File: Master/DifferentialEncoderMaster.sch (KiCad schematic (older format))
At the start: 7 parts

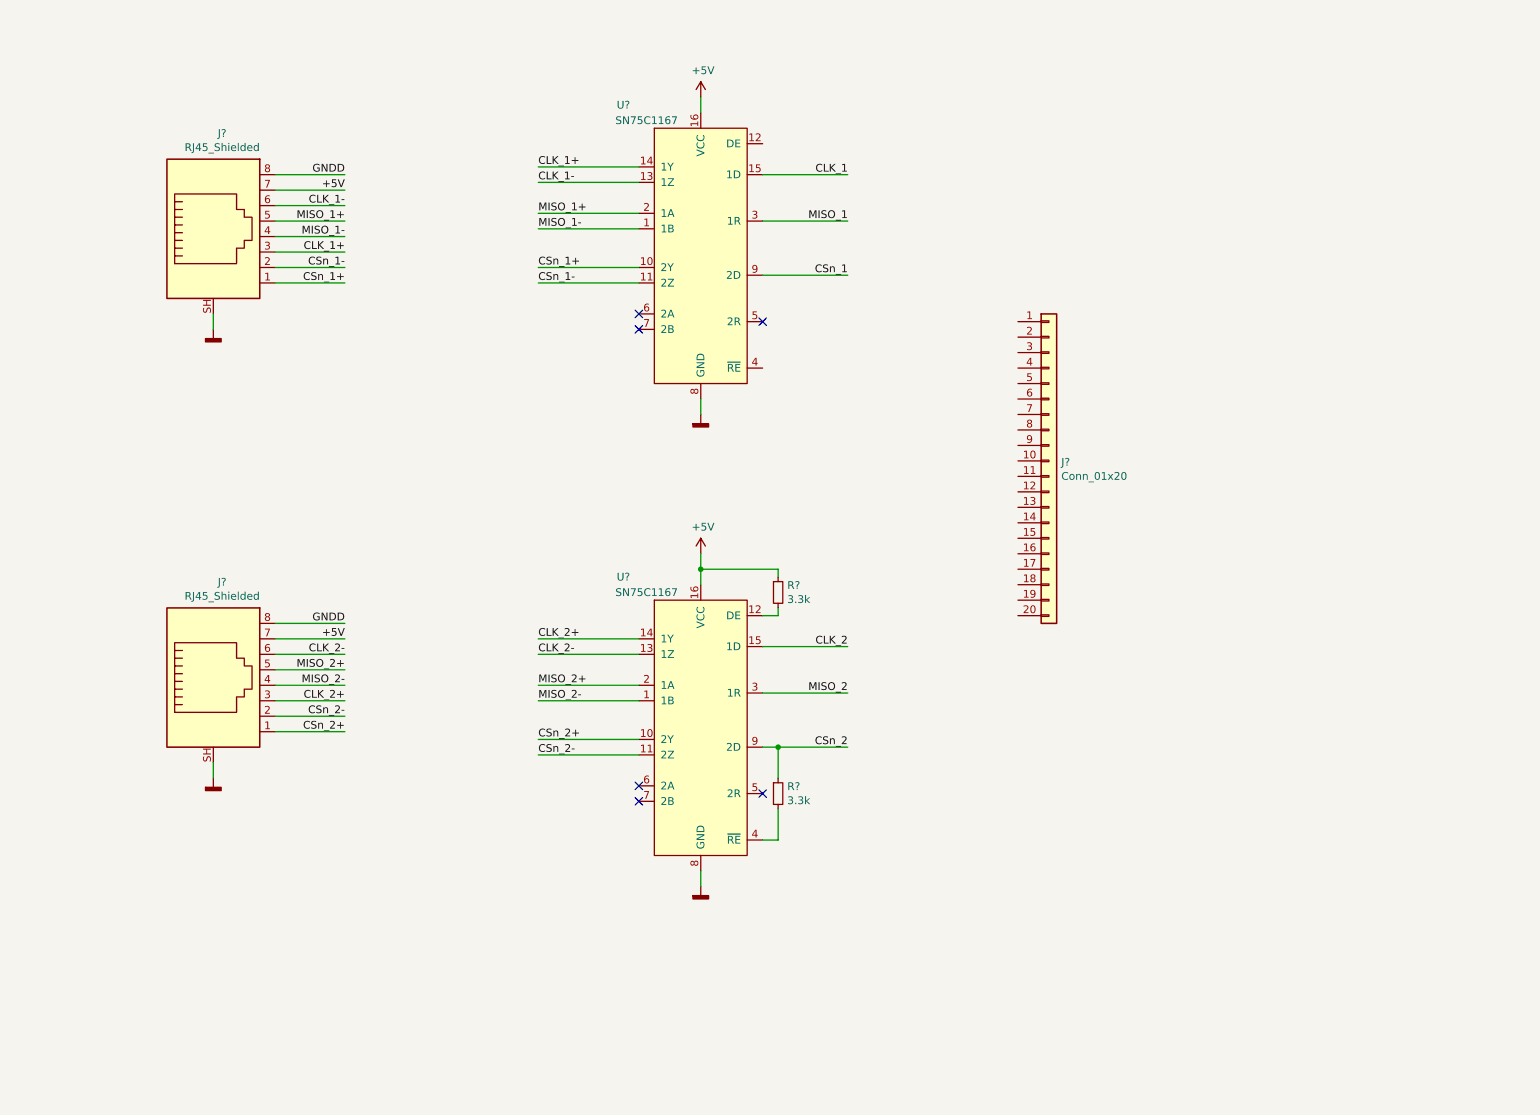
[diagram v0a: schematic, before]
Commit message: Make ODrive side full board length, add diff. incremental
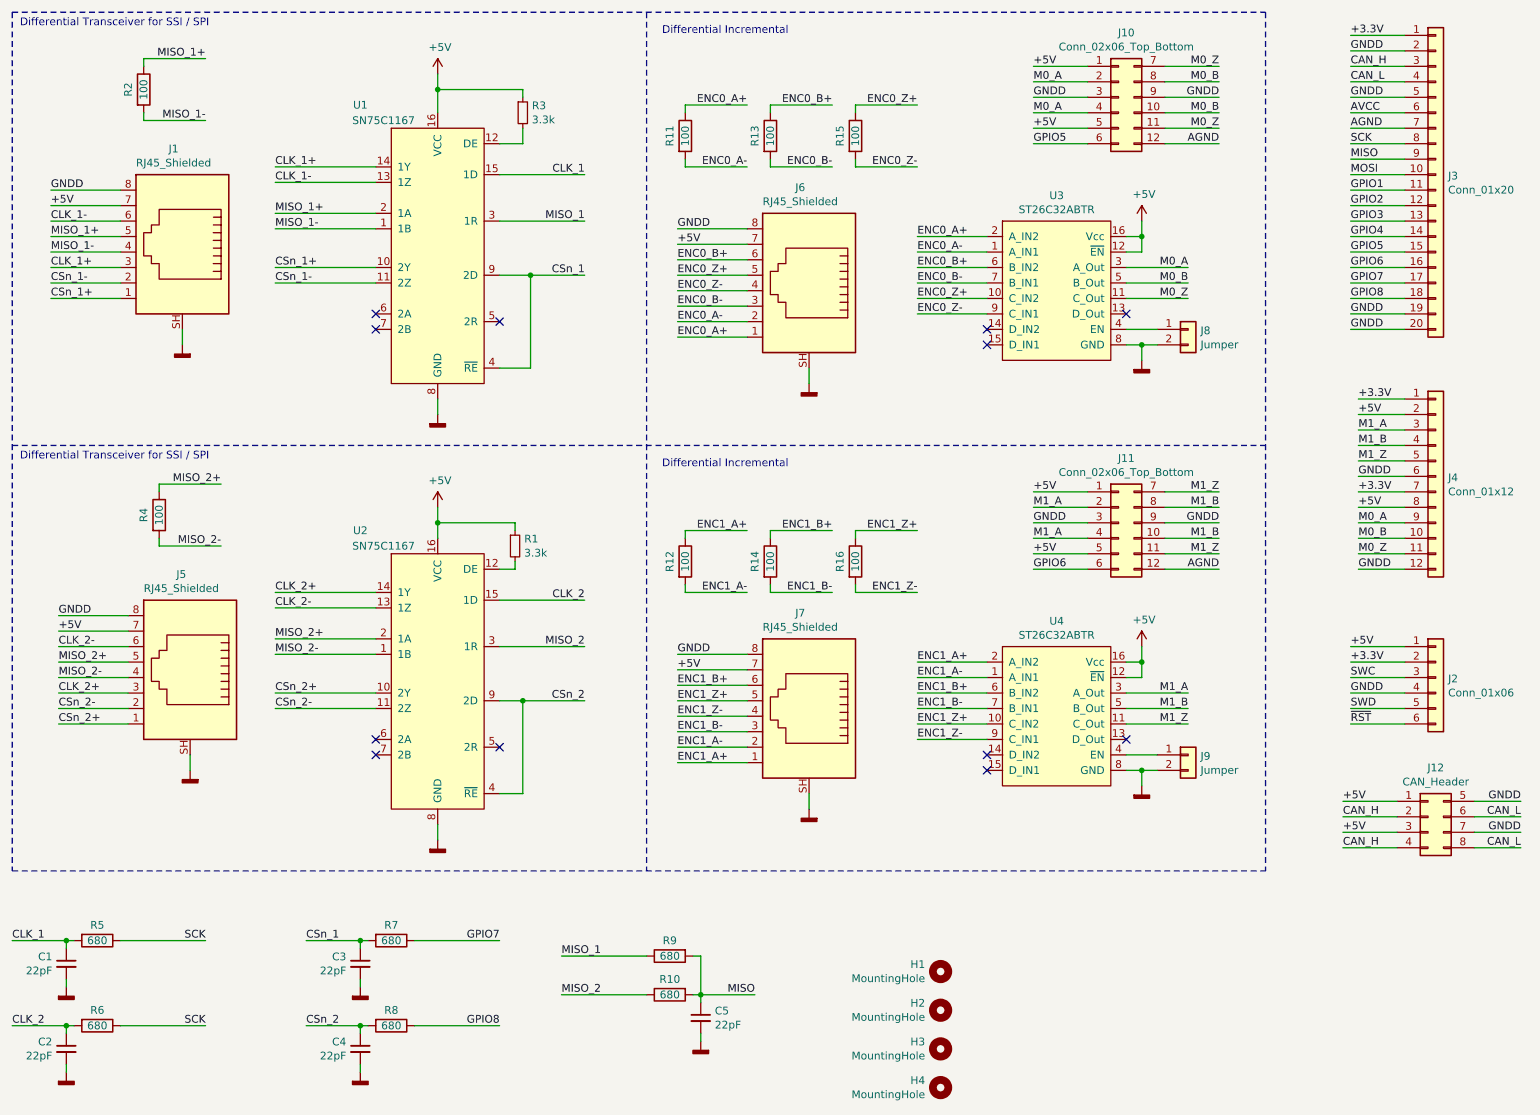
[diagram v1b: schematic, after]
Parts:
- removed J? (x2): RJ45_Shielded, symbol Connector:RJ45_Shielded
- removed R?: 3.3k, symbol Device:R_Small
- added C1, C2, C3, C4, C5: 22pF, Capacitor_SMD:C_0603_1608Metric, symbol Device:C_Small
- added H1, H2, H3, H4: MountingHole, MountingHole:MountingHole_3.2mm_M3, symbol Mechanical:MountingHole
- added J1, J5, J6, J7: RJ45_Shielded, Connector_RJ:RJ45_Amphenol_RJHSE538X, symbol Connector:RJ45_Shielded
- added J10, J11: Conn_02x06_Top_Bottom, Connector_Molex:Molex_Nano-Fit_105310-xx12_2x06_P2.50mm_Vertical, symbol Connector_Generic:Conn_02x06_Top_Bottom
- added J12: CAN_Header, Connector_Molex:Molex_Nano-Fit_105310-xx08_2x04_P2.50mm_Vertical, symbol Connector_Generic:Conn_02x04_Top_Bottom
- added J2: Conn_01x06, Connector_PinSocket_2.54mm:PinSocket_1x06_P2.54mm_Vertical, symbol Connector_Generic:Conn_01x06
- added J4: Conn_01x12, Connector_PinSocket_2.54mm:PinSocket_1x12_P2.54mm_Vertical, symbol Connector_Generic:Conn_01x12
- added J8, J9: Jumper, Connector_PinHeader_2.54mm:PinHeader_1x02_P2.54mm_Vertical, symbol Connector_Generic:Conn_01x02
- added R10, R5, R6, R7, R8, R9: 680, Resistor_SMD:R_0603_1608Metric, symbol Device:R
- added R11, R12, R13, R14, R15, R16, R2, R4: 100, Resistor_SMD:R_0603_1608Metric, symbol Device:R
- added R3: 3.3k, Resistor_SMD:R_0603_1608Metric, symbol Device:R_Small
- added U3, U4: ST26C32ABTR, Package_SO:TSSOP-16_4.4x5mm_P0.65mm, symbol Wetmelon:ST26C32ABTR
- J3: renamed from J?; footprint (none) -> Connector_PinSocket_2.54mm:PinSocket_1x20_P2.54mm_Vertical
- R1: renamed from R?; footprint (none) -> Resistor_SMD:R_0603_1608Metric
- U1, U2: renamed from U?; footprint (none) -> Package_SO:TSSOP-16_4.4x5mm_P0.65mm
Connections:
- net +5V: now also J1.7, J10.1 (Pin_1), J10.5 (Pin_5), J11.1 (Pin_1), J11.5 (Pin_5), J12.1 (Pin_1), J12.3 (Pin_3), J2.1 (Pin_1), J4.2 (Pin_2), J4.8 (Pin_8), J5.7, J6.7, J7.7, R3.1, U3.12 (~EN), U3.16 (Vcc), U4.12 (~EN), U4.16 (Vcc)
- net CLK_1: now also C1.1, R5.2
- net CLK_1+: now also J1.3
- net CLK_1-: now also J1.6
- net CLK_2: now also C2.1, R6.2
- net CLK_2+: now also J5.3
- net CLK_2-: now also J5.6
- net CSn_1: now also U1.4 (~RE), C3.1, R7.2
- net CSn_1+: now also J1.1
- net CSn_1-: now also J1.2
- net CSn_2: now also U2.4 (~RE), C4.1, R8.2
- net CSn_2+: now also J5.1
- net CSn_2-: now also J5.2
- net GNDD: now also J3.19 (Pin_19), J3.2 (Pin_2), J3.20 (Pin_20), J3.5 (Pin_5), C1.2, C2.2, C3.2, C4.2, C5.2, J1.8, J1.SH, J10.3 (Pin_3), J10.9 (Pin_9), J11.3 (Pin_3), J11.9 (Pin_9), J12.5 (Pin_5), J12.7 (Pin_7), J2.4 (Pin_4), J4.12 (Pin_12), J4.6 (Pin_6), J5.8, J5.SH, J6.8, J6.SH, J7.8, J7.SH, J8.2 (Pin_2), J9.2 (Pin_2), U3.8 (GND), U4.8 (GND)
- net MISO_1: now also R9.1
- net MISO_1+: now also J1.5, R2.1
- net MISO_1-: now also J1.4, R2.2
- net MISO_2: now also R10.1
- net MISO_2+: now also J5.5, R4.1
- net MISO_2-: now also J5.4, R4.2
- net +3.3V: now reaches J3.1 (Pin_1)
- net +3.3V: now also J2.2 (Pin_2), J4.1 (Pin_1), J4.7 (Pin_7)
- net MOSI: now reaches J3.10 (Pin_10)
- net GPIO1: now reaches J3.11 (Pin_11)
- net GPIO2: now reaches J3.12 (Pin_12)
- net GPIO3: now reaches J3.13 (Pin_13)
- net GPIO4: now reaches J3.14 (Pin_14)
- net GPIO5: now reaches J3.15 (Pin_15)
- net GPIO5: now also J10.6 (Pin_6)
- net GPIO6: now reaches J3.16 (Pin_16)
- net GPIO6: now also J11.6 (Pin_6)
- net GPIO7: now reaches J3.17 (Pin_17)
- net GPIO7: now also R7.1
- net GPIO8: now reaches J3.18 (Pin_18)
- net GPIO8: now also R8.1
- net CAN_H: now reaches J3.3 (Pin_3)
- net CAN_H: now also J12.2 (Pin_2), J12.4 (Pin_4)
- net CAN_L: now reaches J3.4 (Pin_4)
- net CAN_L: now also J12.6 (Pin_6), J12.8 (Pin_8)
- net AVCC: now reaches J3.6 (Pin_6)
- net AGND: now reaches J3.7 (Pin_7)
- net AGND: now also J10.12 (Pin_12), J11.12 (Pin_12)
- net SCK: now reaches J3.8 (Pin_8)
- net SCK: now also R5.1, R6.1
- net MISO: now reaches J3.9 (Pin_9)
- net MISO: now also C5.1, R10.2, R9.2
- net at U1.12 (DE): now also R3.2
- new net: J8.1 (Pin_1), U3.4 (EN)
- new net: J9.1 (Pin_1), U4.4 (EN)
- new net ENC0_A+: J6.1, R11.1, U3.2 (A_IN2)
- new net ENC0_A-: J6.2, R11.2, U3.1 (A_IN1)
- new net ENC0_B+: J6.6, R13.1, U3.6 (B_IN2)
- new net ENC0_B-: J6.3, R13.2, U3.7 (B_IN1)
- new net ENC0_Z+: J6.5, R15.1, U3.10 (C_IN2)
- new net ENC0_Z-: J6.4, R15.2, U3.9 (C_IN1)
- new net ENC1_A+: J7.1, R12.1, U4.2 (A_IN2)
- new net ENC1_A-: J7.2, R12.2, U4.1 (A_IN1)
- new net ENC1_B+: J7.6, R14.1, U4.6 (B_IN2)
- new net ENC1_B-: J7.3, R14.2, U4.7 (B_IN1)
- new net ENC1_Z+: J7.5, R16.1, U4.10 (C_IN2)
- new net ENC1_Z-: J7.4, R16.2, U4.9 (C_IN1)
- new net M0_A: J10.2 (Pin_2), J10.4 (Pin_4), J4.9 (Pin_9), U3.3 (A_Out)
- new net M0_B: J10.10 (Pin_10), J10.8 (Pin_8), J4.10 (Pin_10), U3.5 (B_Out)
- new net M0_Z: J10.11 (Pin_11), J10.7 (Pin_7), J4.11 (Pin_11), U3.11 (C_Out)
- new net M1_A: J11.2 (Pin_2), J11.4 (Pin_4), J4.3 (Pin_3), U4.3 (A_Out)
- new net M1_B: J11.10 (Pin_10), J11.8 (Pin_8), J4.4 (Pin_4), U4.5 (B_Out)
- new net M1_Z: J11.11 (Pin_11), J11.7 (Pin_7), J4.5 (Pin_5), U4.11 (C_Out)
- new net SWC: J2.3 (Pin_3)
- new net SWD: J2.5 (Pin_5)
- new net ~RST: J2.6 (Pin_6)
- no-connect marks 6 -> 12
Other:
- note added: "Differential Incremental"
- note added: "Differential Transceiver for SSI / SPI"
- moved on the sheet: J3, R1, U1, U2

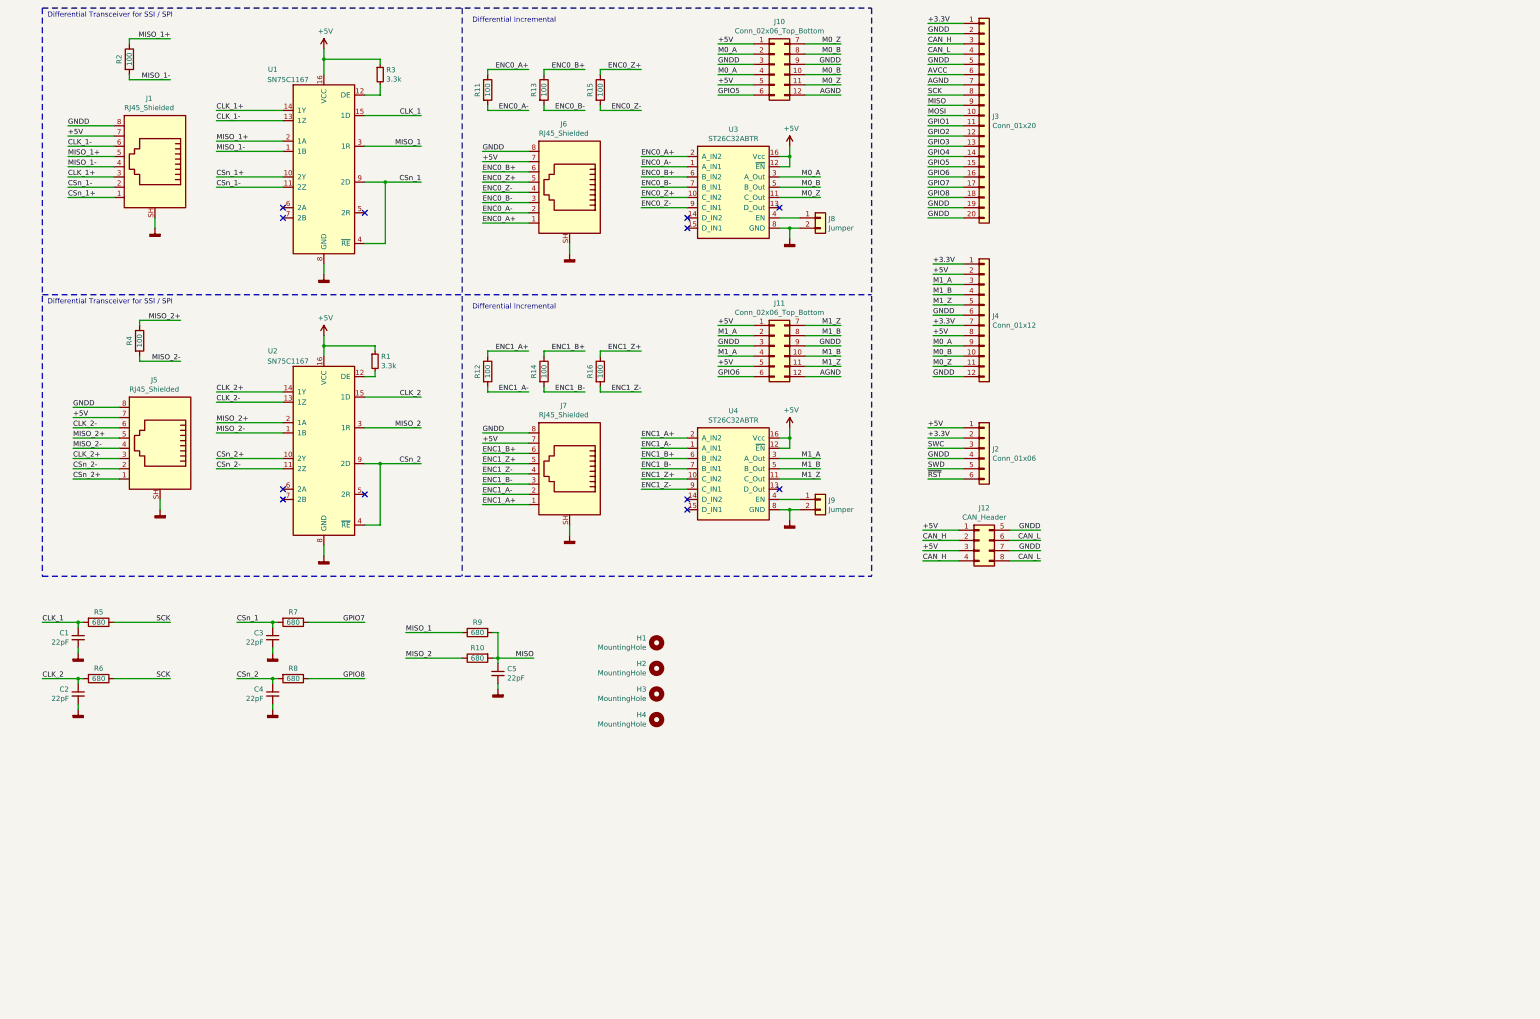
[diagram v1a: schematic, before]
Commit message: Add digital isolators
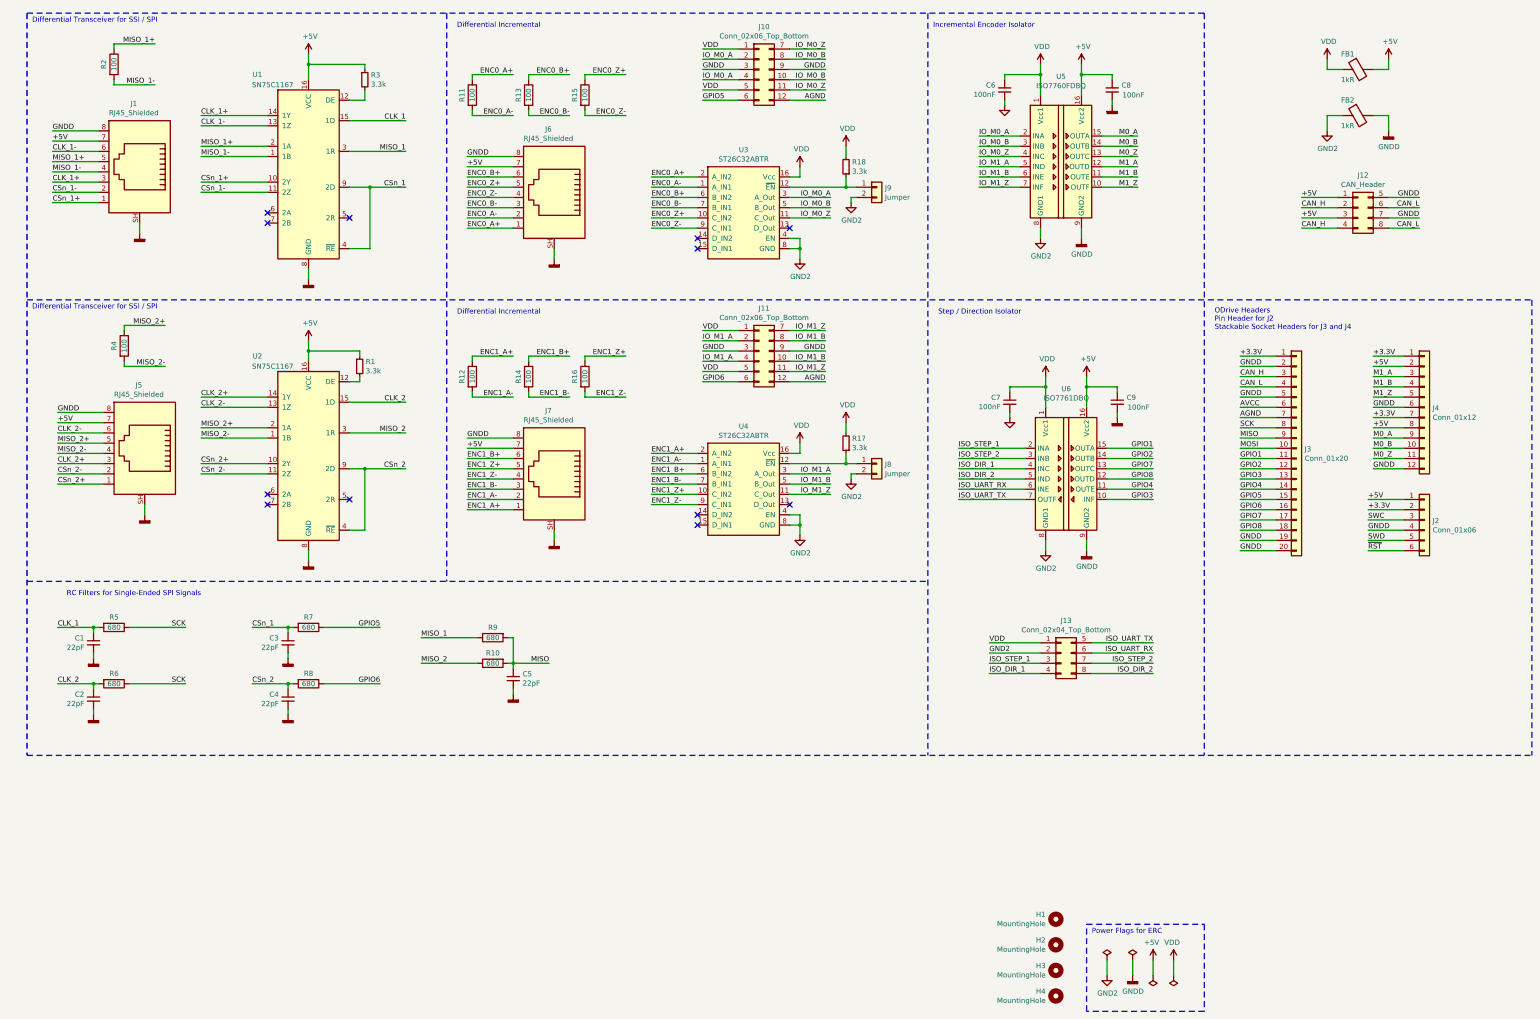
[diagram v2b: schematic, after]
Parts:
- added C6, C7, C8, C9: 100nF, Capacitor_SMD:C_0603_1608Metric, symbol Device:C_Small
- added FB1, FB2: 1kR, symbol Device:Ferrite_Bead
- added J13: Conn_02x04_Top_Bottom, symbol Connector_Generic:Conn_02x04_Top_Bottom
- added R17, R18: 3.3k, symbol Device:R_Small
- added U5: ISO7760FDBQ, Package_SO:SSOP-16_3.9x4.9mm_P0.635mm, symbol Isolator:ISO7760FDBQ
- added U6: ISO7761DBQ, Package_SO:SSOP-16_3.9x4.9mm_P0.635mm, symbol Isolator:ISO7761DBQ
- J8, J9: footprint Connector_PinHeader_2.54mm:PinHeader_1x02_P2.54mm_Vertical -> (none)
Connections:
- net +5V: now also C8.1, C9.1, FB1.2, U5.16 (Vcc2), U6.16 (Vcc2); no longer J10.1 (Pin_1), J10.5 (Pin_5), J11.1 (Pin_1), J11.5 (Pin_5), U3.12 (~EN), U3.16 (Vcc), U4.12 (~EN), U4.16 (Vcc)
- net GNDD: now also C8.2, C9.2, FB2.2, U5.9 (GND2), U6.9 (GND2); no longer J8.2 (Pin_2), J9.2 (Pin_2), U3.8 (GND), U4.8 (GND)
- net GPIO1: now also U6.15 (OUTA)
- net GPIO2: now also U6.14 (OUTB)
- net GPIO3: now also U6.10 (INF)
- net GPIO4: now also U6.11 (OUTE)
- net GPIO5: now also R7.1
- net GPIO6: now also R8.1
- net GPIO7: now also U6.13 (OUTC); no longer R7.1
- net GPIO8: now also U6.12 (OUTD); no longer R8.1
- net M0_A: now also U5.15 (OUTA); no longer J10.2 (Pin_2), J10.4 (Pin_4), U3.3 (A_Out)
- net M0_B: now also U5.14 (OUTB); no longer J10.10 (Pin_10), J10.8 (Pin_8), U3.5 (B_Out)
- net M0_Z: now also U5.13 (OUTC); no longer J10.11 (Pin_11), J10.7 (Pin_7), U3.11 (C_Out)
- net M1_A: now also U5.12 (OUTD); no longer J11.2 (Pin_2), J11.4 (Pin_4), U4.3 (A_Out)
- net M1_B: now also U5.11 (OUTE); no longer J11.10 (Pin_10), J11.8 (Pin_8), U4.5 (B_Out)
- net M1_Z: now also U5.10 (OUTF); no longer J11.11 (Pin_11), J11.7 (Pin_7), U4.11 (C_Out)
- net at J8.1 (Pin_1): now also U4.12 (~EN), R17.1; no longer U3.4 (EN)
- net at J9.1 (Pin_1): now also U3.12 (~EN), R18.1; no longer U4.4 (EN)
- new net GND2: C6.2, C7.2, FB2.1, J13.2 (Pin_2), J8.2 (Pin_2), J9.2 (Pin_2), U3.4 (EN), U3.8 (GND), U4.4 (EN), U4.8 (GND), U5.8 (GND1), U6.8 (GND1)
- new net IO_M0_A: J10.2 (Pin_2), J10.4 (Pin_4), U3.3 (A_Out), U5.2 (INA)
- new net IO_M0_B: J10.10 (Pin_10), J10.8 (Pin_8), U3.5 (B_Out), U5.3 (INB)
- new net IO_M0_Z: J10.11 (Pin_11), J10.7 (Pin_7), U3.11 (C_Out), U5.4 (INC)
- new net IO_M1_A: J11.2 (Pin_2), J11.4 (Pin_4), U4.3 (A_Out), U5.5 (IND)
- new net IO_M1_B: J11.10 (Pin_10), J11.8 (Pin_8), U4.5 (B_Out), U5.6 (INE)
- new net IO_M1_Z: J11.11 (Pin_11), J11.7 (Pin_7), U4.11 (C_Out), U5.7 (INF)
- new net ISO_DIR_1: J13.4 (Pin_4), U6.4 (INC)
- new net ISO_DIR_2: J13.8 (Pin_8), U6.5 (IND)
- new net ISO_STEP_1: J13.3 (Pin_3), U6.2 (INA)
- new net ISO_STEP_2: J13.7 (Pin_7), U6.3 (INB)
- new net ISO_UART_RX: J13.6 (Pin_6), U6.6 (INE)
- new net ISO_UART_TX: J13.5 (Pin_5), U6.7 (OUTF)
- new net VDD: C6.1, C7.1, FB1.1, J10.1 (Pin_1), J10.5 (Pin_5), J11.1 (Pin_1), J11.5 (Pin_5), J13.1 (Pin_1), R17.2, R18.2, U3.16 (Vcc), U4.16 (Vcc), U5.1 (Vcc1), U6.1 (Vcc1)
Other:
- note added: "Incremental Encoder Isolator"
- note added: "ODrive Headers\nPin Header for J2\nStackable Socket Headers for J3 and J4"
- note added: "Power Flags for ERC"
- note added: "RC Filters for Single-Ended SPI Signals"
- note added: "Step / Direction Isolator"
- moved on the sheet: C1, C2, C3, C4, C5, H1, H2, H3, H4, J1, J10, J11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
